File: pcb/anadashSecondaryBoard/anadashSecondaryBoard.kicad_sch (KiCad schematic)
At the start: 14 parts, among them J5 DisplayConnector, J6 LeftKeyConnector, J7 RightKeyConnector, J8 EncoderConnector, SW1 SW_Push, SW2 SW_Push, SW3 SW_Push, SW4 SW_Push, SW5 SW_Push, SW6 SW_Push, SW7 SW_Push, SW8 SW_Push, SW9 RotaryEncoder_Switch_MP, U2 ER_OLEDM0.91_1x-I2C

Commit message: Reorganizing into two different projects
Kicad doenst allow two PCBs
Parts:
- renumbered SW1 to SW2, SW2 to SW3, SW3 to SW4, SW4 to SW5, SW5 to SW6, SW6 to SW7, SW7 to SW8, SW8 to SW9
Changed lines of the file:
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@@
+				)
+			)
+			(project "anadashSecondaryBoard"
+				(path "/4afd32ea-561a-4b0e-b8bd-b5545b1531de"
+					(reference "#PWR022")
+					(unit 1)
 				)
 			)
@@
 				)
 			)
-			(project "switchesanddisplay"
+			(project "anadashSecondaryBoard"
 				(path "/4afd32ea-561a-4b0e-b8bd-b5545b1531de"
 					(reference "SW9")
@@
 		(dnp no)
 		(fields_autoplaced yes)
-		(property "Reference" "SW5"
+		(property "Reference" "SW6"
 			(at 59.69 100.33 0)
 			(show_name no)
@@
 				)
 			)
-			(project "switchesanddisplay"
+			(project "anadashSecondaryBoard"
 				(path "/4afd32ea-561a-4b0e-b8bd-b5545b1531de"
 					(reference "SW6")
@@
 		(dnp no)
 		(fields_autoplaced yes)
-		(property "Reference" "SW7"
+		(property "Reference" "SW8"
 			(at 59.69 120.65 0)
 			(show_name no)
@@
 				)
 			)
-			(project "switchesanddisplay"
+			(project "anadashSecondaryBoard"
 				(path "/4afd32ea-561a-4b0e-b8bd-b5545b1531de"
 					(reference "SW8")
@@
 		(dnp no)
 		(fields_autoplaced yes)
-		(property "Reference" "SW8"
+		(property "Reference" "SW9"
 			(at 59.69 130.81 0)
 			(show_name no)
@@
 				)
 			)
-			(project "switchesanddisplay"
+			(project "anadashSecondaryBoard"
 				(path "/4afd32ea-561a-4b0e-b8bd-b5545b1531de"
 					(reference "SW9")
@@
 			(project "anadash_pcb"
 				(path "/356b9cf0-7532-4174-862f-41594407df39"
+					(reference "J8")
+					(unit 1)
+				)
+			)
+			(project "anadashSecondaryBoard"
+				(path "/4afd32ea-561a-4b0e-b8bd-b5545b1531de"
 					(reference "J8")
 					(unit 1)
@@
 				)
 			)
-			(project "switchesanddisplay"
+			(project "anadashSecondaryBoard"
 				(path "/4afd32ea-561a-4b0e-b8bd-b5545b1531de"
 					(reference "U2")
@@
 		(dnp no)
 		(fields_autoplaced yes)
-		(property "Reference" "#PWR023"
+		(property "Reference" "#PWR017"
 			(at 68.58 109.22 0)
 			(hide yes)
@@
 				)
 			)
-			(project "switchesanddisplay"
+			(project "anadashSecondaryBoard"
 				(path "/4afd32ea-561a-4b0e-b8bd-b5545b1531de"
 					(reference "#PWR017")
@@
 		(dnp no)
 		(fields_autoplaced yes)
-		(property "Reference" "SW4"
+		(property "Reference" "SW5"
 			(at 59.69 90.17 0)
 			(show_name no)
@@
 				)
 			)
-			(project "switchesanddisplay"
+			(project "anadashSecondaryBoard"
 				(path "/4afd32ea-561a-4b0e-b8bd-b5545b1531de"
 					(reference "SW5")
@@
 		(dnp no)
 		(fields_autoplaced yes)
-		(property "Reference" "SW3"
+		(property "Reference" "SW4"
 			(at 59.69 80.01 0)
 			(show_name no)
@@
 				)
 			)
-			(project "switchesanddisplay"
+			(project "anadashSecondaryBoard"
 				(path "/4afd32ea-561a-4b0e-b8bd-b5545b1531de"
 					(reference "SW4")
@@
 		(dnp no)
 		(fields_autoplaced yes)
-		(property "Reference" "SW6"
+		(property "Reference" "SW7"
 			(at 59.69 110.49 0)
 			(show_name no)
@@
 				)
 			)
-			(project "switchesanddisplay"
+			(project "anadashSecondaryBoard"
 				(path "/4afd32ea-561a-4b0e-b8bd-b5545b1531de"
 					(reference "SW7")
@@
 				)
 			)
+			(project "anadashSecondaryBoard"
+				(path "/4afd32ea-561a-4b0e-b8bd-b5545b1531de"
+					(reference "J6")
+					(unit 1)
+				)
+			)
 		)
 	)
@@
 		(dnp no)
 		(fields_autoplaced yes)
-		(property "Reference" "SW1"
+		(property "Reference" "SW2"
 			(at 59.69 59.69 0)
 			(show_name no)
@@
 				)
 			)
-			(project "switchesanddisplay"
+			(project "anadashSecondaryBoard"
 				(path "/4afd32ea-561a-4b0e-b8bd-b5545b1531de"
 					(reference "SW2")
@@
 				)
 			)
-			(project "switchesanddisplay"
+			(project "anadashSecondaryBoard"
 				(path "/4afd32ea-561a-4b0e-b8bd-b5545b1531de"
 					(reference "#PWR019")
@@
 			(project "anadash_pcb"
 				(path "/356b9cf0-7532-4174-862f-41594407df39"
+					(reference "#PWR021")
+					(unit 1)
+				)
+			)
+			(project "anadashSecondaryBoard"
+				(path "/4afd32ea-561a-4b0e-b8bd-b5545b1531de"
 					(reference "#PWR021")
 					(unit 1)
@@
 				)
 			)
+			(project "anadashSecondaryBoard"
+				(path "/4afd32ea-561a-4b0e-b8bd-b5545b1531de"
+					(reference "J5")
+					(unit 1)
+				)
+			)
 		)
 	)
@@
 		(dnp no)
 		(fields_autoplaced yes)
-		(property "Reference" "SW2"
+		(property "Reference" "SW3"
 			(at 59.69 69.85 0)
 			(show_name no)
@@
 				)
 			)
-			(project "switchesanddisplay"
+			(project "anadashSecondaryBoard"
 				(path "/4afd32ea-561a-4b0e-b8bd-b5545b1531de"
 					(reference "SW3")
@@
 				)
 			)
+			(project "anadashSecondaryBoard"
+				(path "/4afd32ea-561a-4b0e-b8bd-b5545b1531de"
+					(reference "#PWR018")
+					(unit 1)
+				)
+			)
 		)
 	)
@@
 		(dnp no)
 		(fields_autoplaced yes)
-		(property "Reference" "#PWR024"
+		(property "Reference" "#PWR018"
 			(at 69.85 173.99 0)
 			(hide yes)
@@
 				)
 			)
-			(project "switchesanddisplay"
+			(project "anadashSecondaryBoard"
 				(path "/4afd32ea-561a-4b0e-b8bd-b5545b1531de"
 					(reference "#PWR018")
@@
 		(dnp no)
 		(fields_autoplaced yes)
-		(property "Reference" "#PWR020"
+		(property "Reference" "#PWR016"
 			(at 44.45 46.99 0)
 			(hide yes)
@@
 				)
 			)
-			(project "switchesanddisplay"
+			(project "anadashSecondaryBoard"
 				(path "/4afd32ea-561a-4b0e-b8bd-b5545b1531de"
 					(reference "#PWR016")
@@
 			(project "anadash_pcb"
 				(path "/356b9cf0-7532-4174-862f-41594407df39"
+					(reference "J7")
+					(unit 1)
+				)
+			)
+			(project "anadashSecondaryBoard"
+				(path "/4afd32ea-561a-4b0e-b8bd-b5545b1531de"
 					(reference "J7")
 					(unit 1)
@@
 	(sheet_instances
 		(path "/"
-			(page "2")
-		)
-	)
+			(page "1")
+		)
+	)
+	(embedded_fonts no)
 )

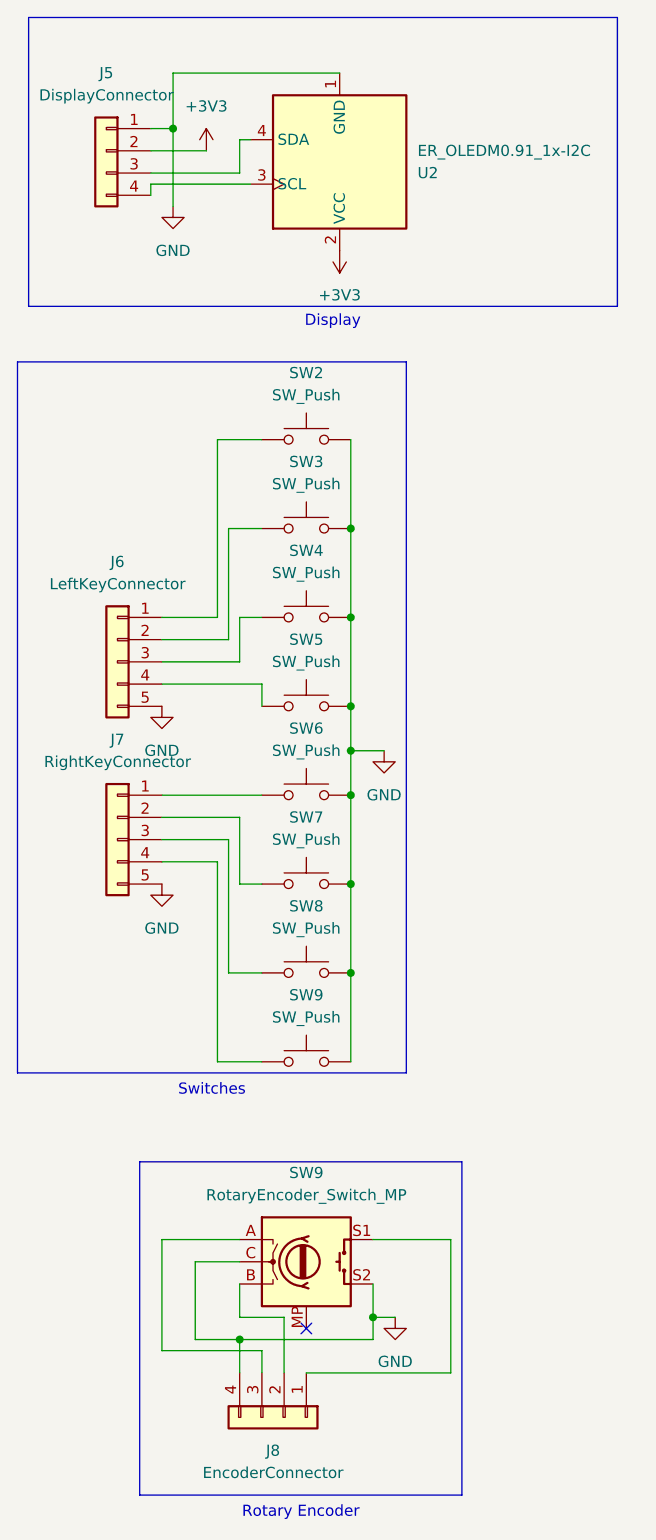
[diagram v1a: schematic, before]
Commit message: Finish the 2nd PCB
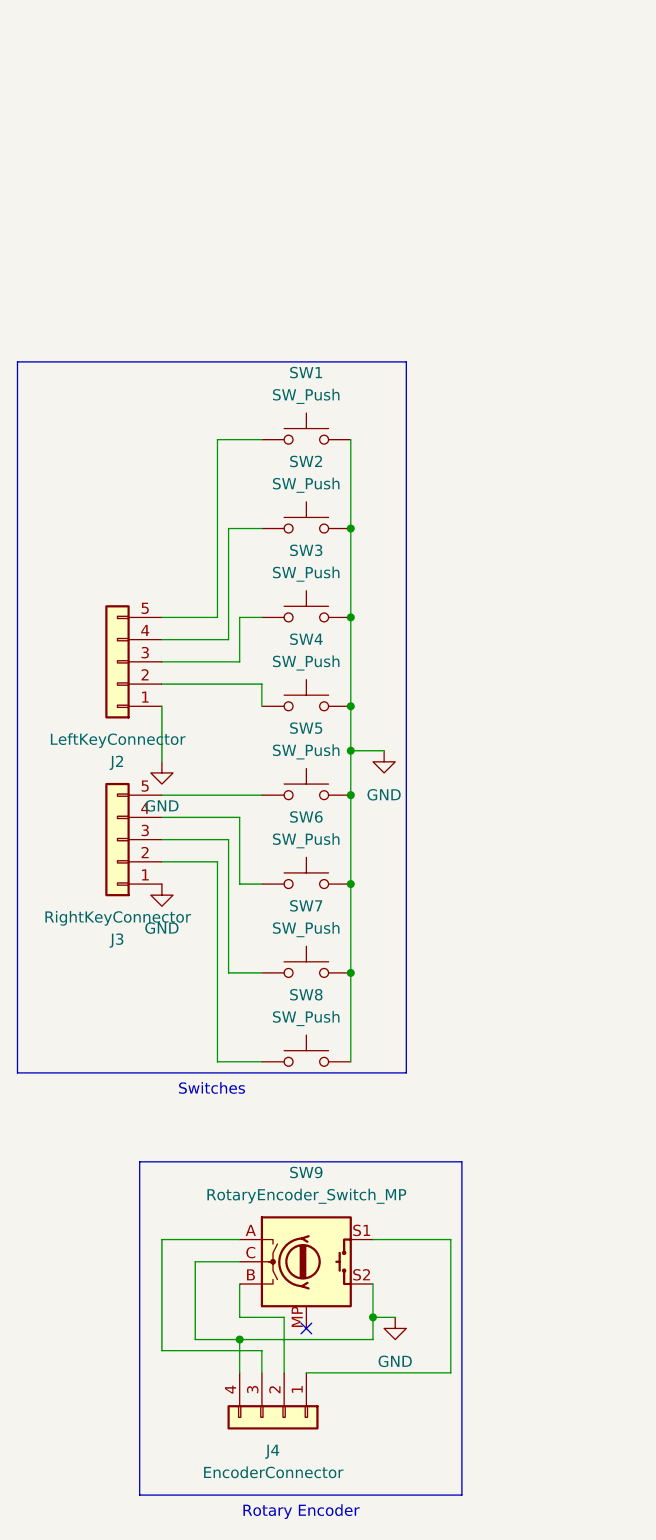
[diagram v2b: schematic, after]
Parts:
- removed J5: DisplayConnector, Connector_JST:JST_XH_B4B-XH-A_1x04_P2.50mm_Vertical, symbol Connector_Generic:Conn_01x04
- removed U2: ER_OLEDM0.91_1x-I2C, Connector_JST:JST_XH_B4B-XH-A_1x04_P2.50mm_Vertical, symbol Display_Graphic:ER_OLEDM0.91_1x-I2C
- SW1: renamed from SW2; footprint Button_Switch_Keyboard:SW_Cherry_MX_1.00u_PCB -> Library:SW_Cherry_MX_1.00u_PCB
- SW2: renamed from SW3; footprint Button_Switch_Keyboard:SW_Cherry_MX_1.00u_PCB -> Library:SW_Cherry_MX_1.00u_PCB
- SW3: renamed from SW4; footprint Button_Switch_Keyboard:SW_Cherry_MX_1.00u_PCB -> Library:SW_Cherry_MX_1.00u_PCB
- SW4: renamed from SW5; footprint Button_Switch_Keyboard:SW_Cherry_MX_1.00u_PCB -> Library:SW_Cherry_MX_1.00u_PCB
- SW5: renamed from SW6; footprint Button_Switch_Keyboard:SW_Cherry_MX_1.00u_PCB -> Library:SW_Cherry_MX_1.00u_PCB
- SW6: renamed from SW7; footprint Button_Switch_Keyboard:SW_Cherry_MX_1.00u_PCB -> Library:SW_Cherry_MX_1.00u_PCB
- SW7: renamed from SW8; footprint Button_Switch_Keyboard:SW_Cherry_MX_1.00u_PCB -> Library:SW_Cherry_MX_1.00u_PCB
- SW8: renamed from SW9; footprint Button_Switch_Keyboard:SW_Cherry_MX_1.00u_PCB -> Library:SW_Cherry_MX_1.00u_PCB
- SW9: footprint Rotary_Encoder:RotaryEncoder_Alps_EC11E-Switch_Vertical_H20mm -> Library:RotaryEncoder_Alps_EC11E-Switch_Vertical_H20mm
- renumbered J6 to J2, J7 to J3, J8 to J4
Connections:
- net GND: now also J2.1 (Pin_1), J3.1 (Pin_1); no longer J2.5 (Pin_5), J3.5 (Pin_5)
- net at SW5.1: now also J3.5 (Pin_5); no longer J3.1 (Pin_1)
- net at SW8.1: now also J3.2 (Pin_2); no longer J3.4 (Pin_4)
- net at SW4.1: now also J2.2 (Pin_2); no longer J2.4 (Pin_4)
- net at SW6.1: now also J3.4 (Pin_4); no longer J3.2 (Pin_2)
- net at SW1.1: now also J2.5 (Pin_5); no longer J2.1 (Pin_1)
- net at SW2.1: now also J2.4 (Pin_4); no longer J2.2 (Pin_2)
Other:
- note removed: "Display"
- moved on the sheet: J2, J3

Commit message: Fixing alignment, improvements to pcb such as silkscreen.
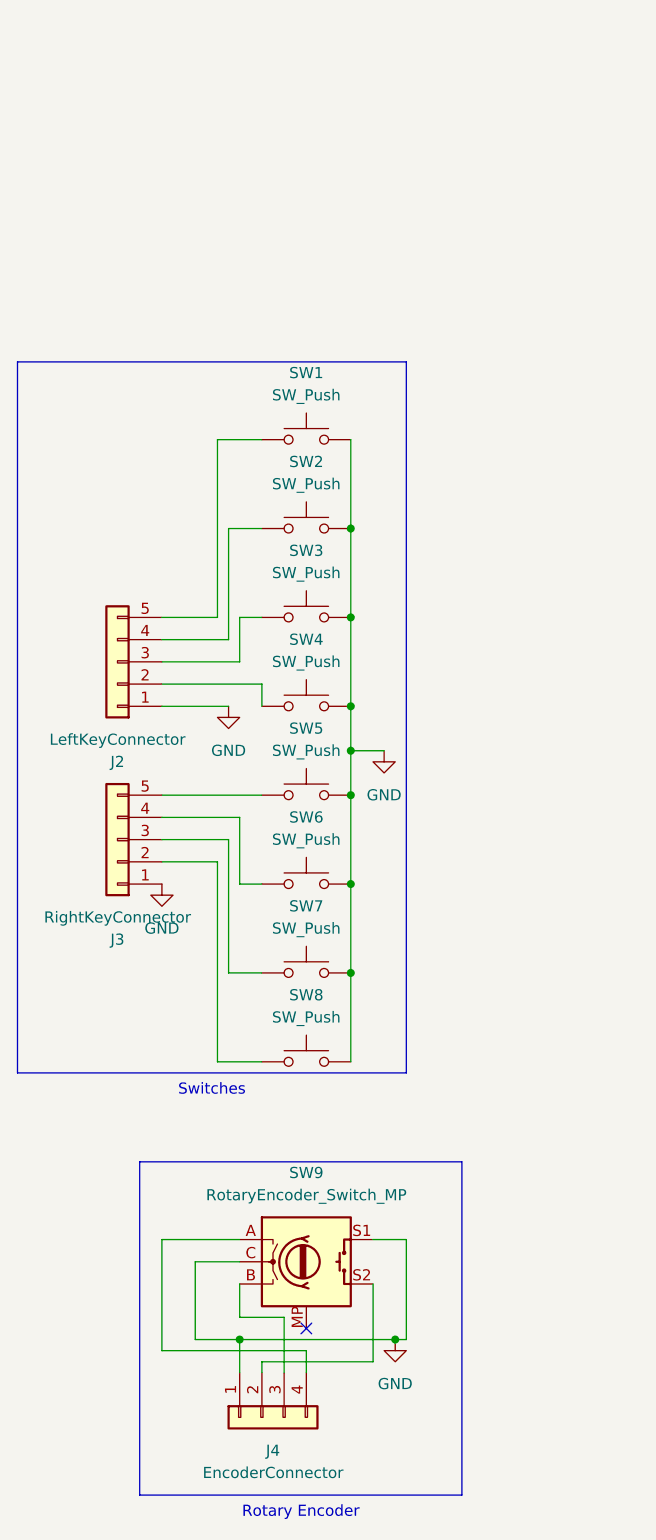
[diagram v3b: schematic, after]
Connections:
- net GND: now also J4.1 (Pin_1), SW9.S1; no longer J4.4 (Pin_4), SW9.S2
- net at SW9.A: now also J4.4 (Pin_4); no longer J4.3 (Pin_3)
- net at SW9.B: now also J4.3 (Pin_3); no longer J4.2 (Pin_2)
- new net: J4.2 (Pin_2), SW9.S2
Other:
- moved on the sheet: J4

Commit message: both pcbs are done, but readme is bad
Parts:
- SW1, SW2, SW3, SW4, SW5, SW6, SW7, SW8: footprint Library:SW_Cherry_MX_1.00u_PCB -> footprints:SW_Cherry_MX_1.00u_PCB
- SW9: footprint Library:RotaryEncoder_Alps_EC11E-Switch_Vertical_H20mm -> footprints:RotaryEncoder_Alps_EC11E-Switch_Vertical_H20mm
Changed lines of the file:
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@@
 			)
 		)
-		(property "Footprint" "Library:RotaryEncoder_Alps_EC11E-Switch_Vertical_H20mm"
+		(property "Footprint" "footprints:RotaryEncoder_Alps_EC11E-Switch_Vertical_H20mm"
 			(at 55.88 157.226 0)
 			(hide yes)
@@
 			)
 		)
-		(property "Footprint" "Library:SW_Cherry_MX_1.00u_PCB"
+		(property "Footprint" "footprints:SW_Cherry_MX_1.00u_PCB"
 			(at 59.69 102.87 0)
 			(hide yes)
@@
 			)
 		)
-		(property "Footprint" "Library:SW_Cherry_MX_1.00u_PCB"
+		(property "Footprint" "footprints:SW_Cherry_MX_1.00u_PCB"
 			(at 59.69 123.19 0)
 			(hide yes)
@@
 			)
 		)
-		(property "Footprint" "Library:SW_Cherry_MX_1.00u_PCB"
+		(property "Footprint" "footprints:SW_Cherry_MX_1.00u_PCB"
 			(at 59.69 133.35 0)
 			(hide yes)
@@
 			)
 		)
-		(property "Footprint" "Library:SW_Cherry_MX_1.00u_PCB"
+		(property "Footprint" "footprints:SW_Cherry_MX_1.00u_PCB"
 			(at 59.69 92.71 0)
 			(hide yes)
@@
 			)
 		)
-		(property "Footprint" "Library:SW_Cherry_MX_1.00u_PCB"
+		(property "Footprint" "footprints:SW_Cherry_MX_1.00u_PCB"
 			(at 59.69 82.55 0)
 			(hide yes)
@@
 			)
 		)
-		(property "Footprint" "Library:SW_Cherry_MX_1.00u_PCB"
+		(property "Footprint" "footprints:SW_Cherry_MX_1.00u_PCB"
 			(at 59.69 113.03 0)
 			(hide yes)
@@
 			)
 		)
-		(property "Footprint" "Library:SW_Cherry_MX_1.00u_PCB"
+		(property "Footprint" "footprints:SW_Cherry_MX_1.00u_PCB"
 			(at 59.69 62.23 0)
 			(hide yes)
@@
 			)
 		)
-		(property "Footprint" "Library:SW_Cherry_MX_1.00u_PCB"
+		(property "Footprint" "footprints:SW_Cherry_MX_1.00u_PCB"
 			(at 59.69 72.39 0)
 			(hide yes)
